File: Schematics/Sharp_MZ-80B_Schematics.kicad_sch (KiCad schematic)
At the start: 0 parts

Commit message: Further updates
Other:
- added sheet CPU Board Circuit (2) (CPU_Board_2.kicad_sch)
- note added: "WORK IN PROGRESS (15/FEB/2026)"
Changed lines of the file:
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@@
 		(comment 4 "Redrawn from Service Manual")
 	)
-	(sheet
-		(at 81.28 17.78)
+	(text "WORK IN PROGRESS\n(15/FEB/2026)"
+		(exclude_from_sim no)
+		(at 183.134 138.684 0)
+		(effects
+			(font
+				(size 10 10)
+			)
+		)
+	)
+	(sheet
+		(at 146.05 17.78)
 		(size 38.1 29.21)
 		(exclude_from_sim no)
@@
 		)
 		(property "Sheetname" "CPU Board Circuits (5)"
-			(at 81.28 17.0684 0)
+			(at 146.05 17.0684 0)
 			(effects
 				(font
@@
 		)
 		(property "Sheetfile" "CPU_Board_5.kicad_sch"
-			(at 81.28 47.5746 0)
-			(effects
-				(font
-					(size 1.27 1.27)
-				)
-				(justify left top)
-			)
-		)
-		(instances
-			(project "Sharp_MZ-80B_Schematics"
-				(path "/8ca4f8f2-2925-48ce-9d44-2cd7cb5f6493"
-					(page "5")
+			(at 146.05 47.5746 0)
+			(effects
+				(font
+					(size 1.27 1.27)
+				)
+				(justify left top)
+			)
+		)
+		(instances
+			(project "Sharp_MZ-80B_Schematics"
+				(path "/8ca4f8f2-2925-48ce-9d44-2cd7cb5f6493"
+					(page "6")
 				)
 			)
@@
 			(project "Sharp_MZ-80B_Schematics"
 				(path "/8ca4f8f2-2925-48ce-9d44-2cd7cb5f6493"
-					(page "6")
+					(page "7")
 				)
 			)
@@
 			(project "Sharp_MZ-80B_Schematics"
 				(path "/8ca4f8f2-2925-48ce-9d44-2cd7cb5f6493"
-					(page "3")
+					(page "10")
 				)
 			)
@@
 			(project "Sharp_MZ-80B_Schematics"
 				(path "/8ca4f8f2-2925-48ce-9d44-2cd7cb5f6493"
-					(page "4")
-				)
-			)
+					(page "9")
+				)
+			)
+		)
+	)
+	(sheet
+		(at 64.77 16.51)
+		(size 45.72 30.48)
+		(exclude_from_sim no)
+		(in_bom yes)
+		(on_board yes)
+		(dnp no)
+		(fields_autoplaced yes)
+		(stroke
+			(width 0.1524)
+			(type solid)
+		)
+		(fill
+			(color 0 0 0 0.0000)
+		)
+		(property "Sheetname" "CPU Board Circuit (2)"
+			(at 64.77 15.7984 0)
+			(effects
+				(font
+					(size 1.27 1.27)
+				)
+				(justify left bottom)
+			)
+		)
+		(property "Sheetfile" "CPU_Board_2.kicad_sch"
+			(at 64.77 47.5746 0)
+			(effects
+				(font
+					(size 1.27 1.27)
+				)
+				(justify left top)
+			)
+		)
+		(instances
+			(project "Sharp_MZ-80B_Schematics"
+				(path "/8ca4f8f2-2925-48ce-9d44-2cd7cb5f6493"
+					(page "3")
+				)
+			)

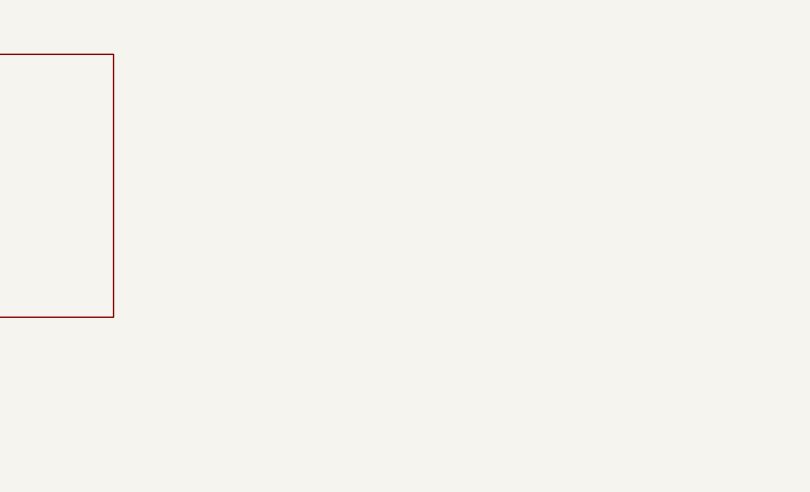
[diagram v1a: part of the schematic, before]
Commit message: Update Sharp_MZ-80B_Schematics.kicad_sch
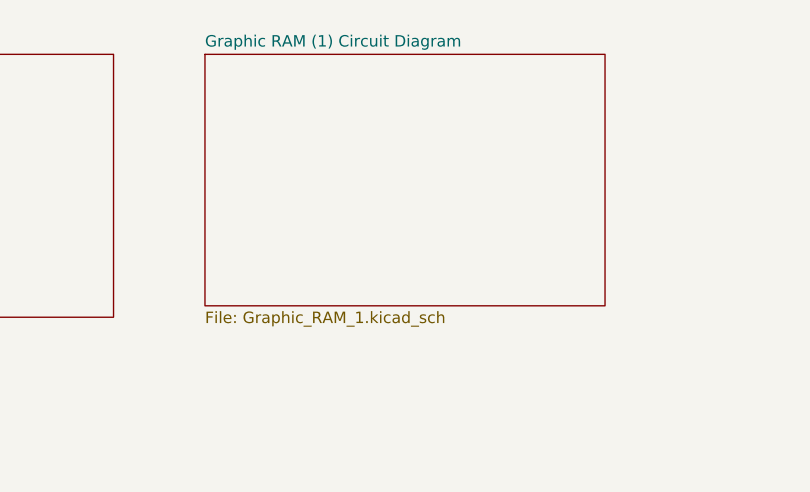
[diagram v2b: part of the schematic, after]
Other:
- added sheet Graphic RAM (1) Circuit Diagram (Graphic_RAM_1.kicad_sch)
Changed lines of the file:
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@@
+		)
+	)
+	(sheet
+		(at 194.31 17.78)
+		(size 44.45 27.94)
+		(exclude_from_sim no)
+		(in_bom yes)
+		(on_board yes)
+		(dnp no)
+		(fields_autoplaced yes)
+		(stroke
+			(width 0.1524)
+			(type solid)
+		)
+		(fill
+			(color 0 0 0 0.0000)
+		)
+		(property "Sheetname" "Graphic RAM (1) Circuit Diagram"
+			(at 194.31 17.0684 0)
+			(effects
+				(font
+					(size 1.27 1.27)
+				)
+				(justify left bottom)
+			)
+		)
+		(property "Sheetfile" "Graphic_RAM_1.kicad_sch"
+			(at 194.31 46.3046 0)
+			(effects
+				(font
+					(size 1.27 1.27)
+				)
+				(justify left top)
+			)
+		)
+		(instances
+			(project "Sharp_MZ-80B_Schematics"
+				(path "/8ca4f8f2-2925-48ce-9d44-2cd7cb5f6493"
+					(page "8")
+				)
+			)
 		)
 	)
